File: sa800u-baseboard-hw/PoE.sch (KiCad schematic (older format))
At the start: 23 parts

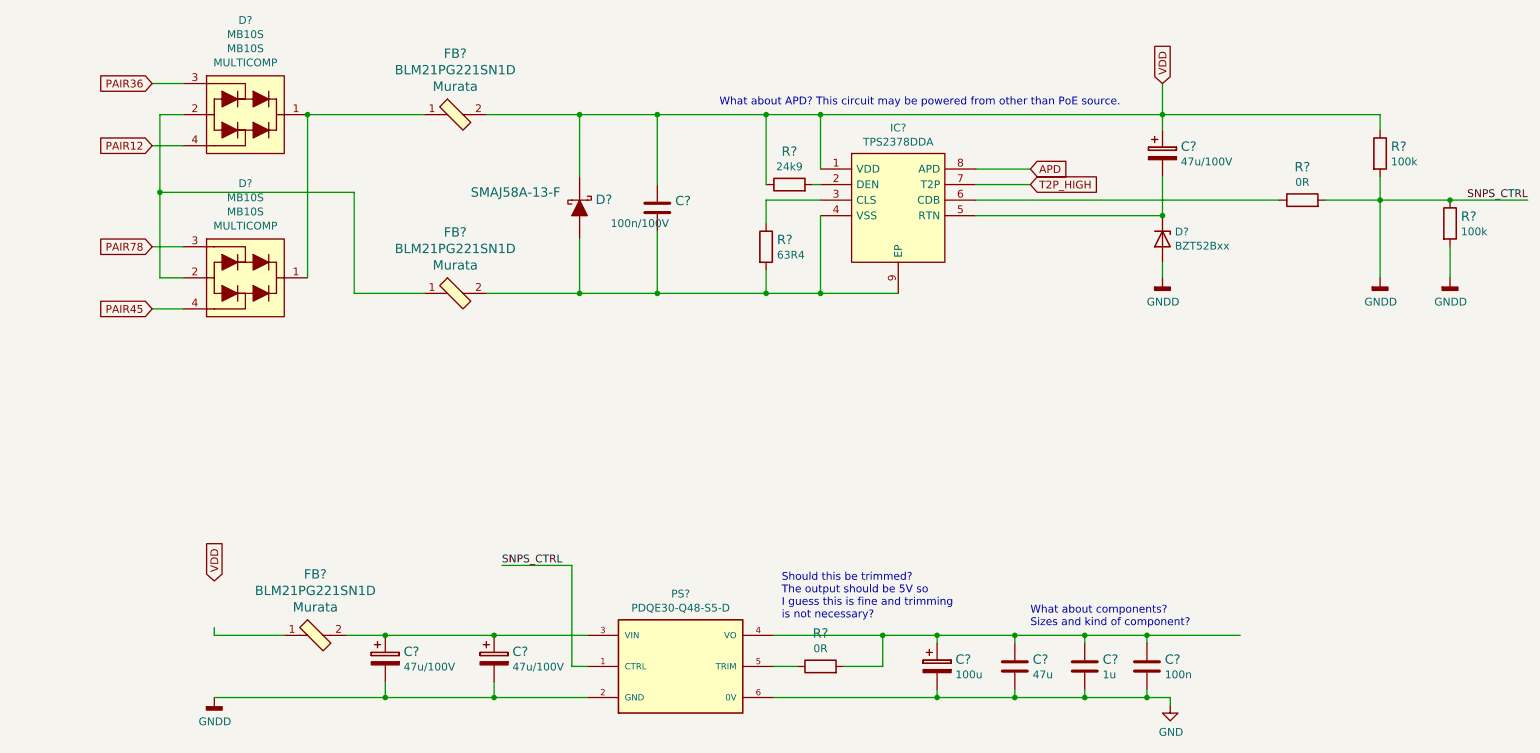
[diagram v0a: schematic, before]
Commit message: added initial version of ethernet controller
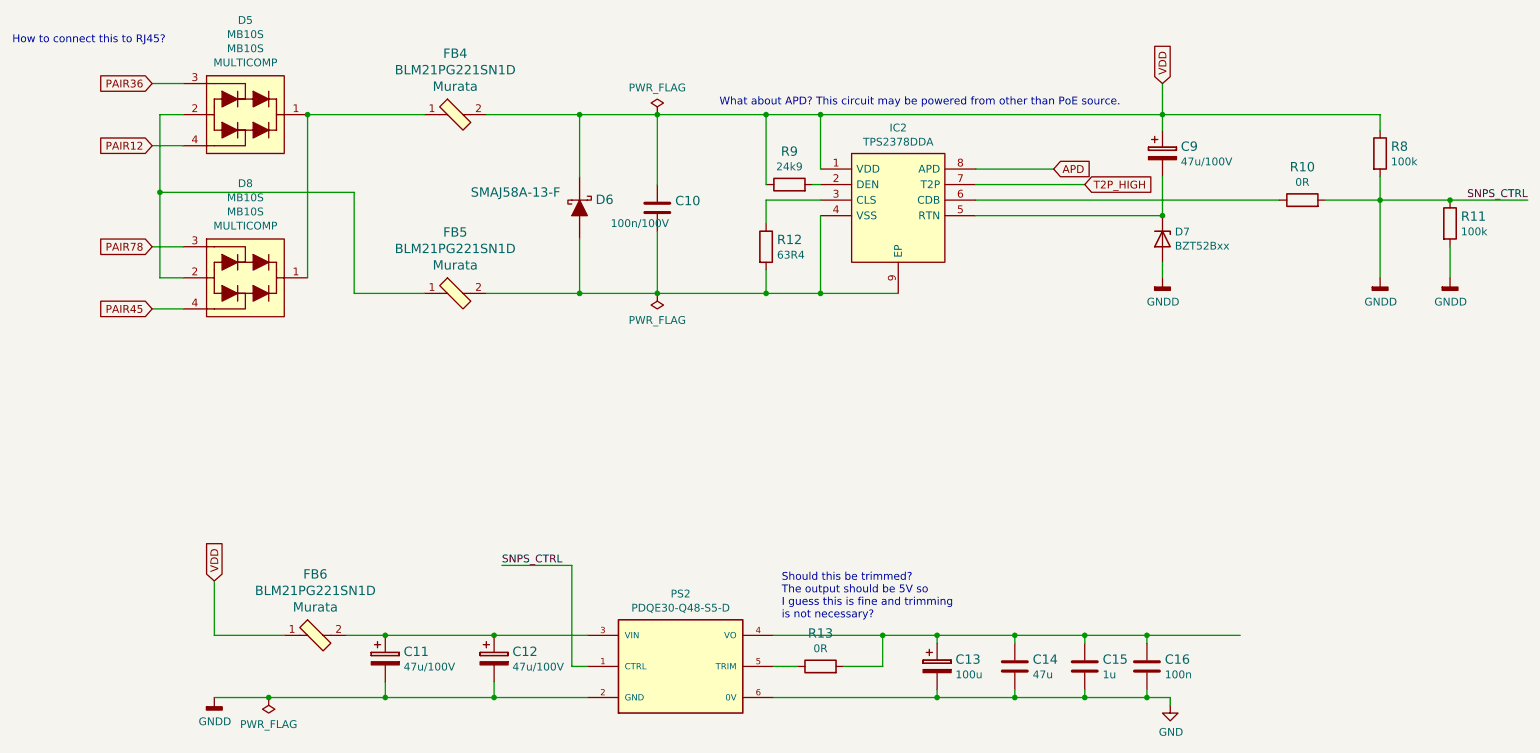
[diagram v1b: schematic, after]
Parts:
- gave numbers to parts that had none: 23
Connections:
- net VDD: now also FB6.1
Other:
- note added: "How to connect this to RJ45?"
- note removed: "What about components? \nSizes and kind of component?"

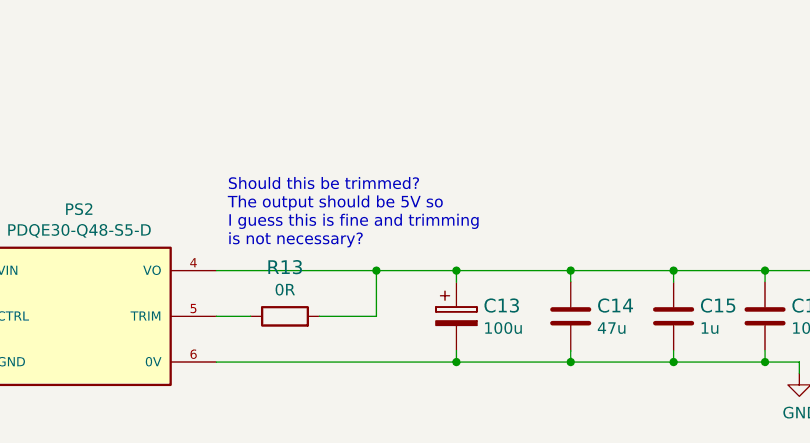
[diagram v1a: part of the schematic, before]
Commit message: added a voltage trimming possibility in PoE circuit
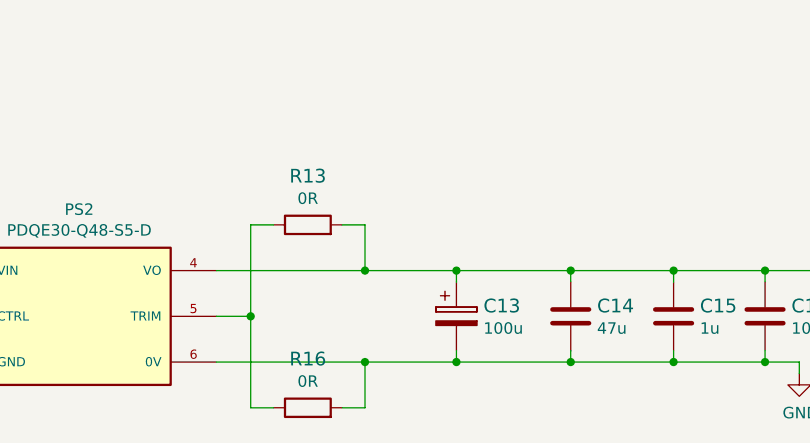
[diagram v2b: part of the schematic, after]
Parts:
- added R16: R_0R_0402, antmicro-footprints:0402-res, symbol antmicroResistors0402:R_0R_0402
- R13: DNP (none) -> DNP
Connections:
- net GND: now also R16.2
- net at PS2.5 (TRIM), R13.1: now also R16.1
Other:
- note removed: "Should this be trimmed? \nThe output should be 5V so\nI guess this is fine and trimming\nis not necessary?"
- moved on the sheet: R13
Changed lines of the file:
@@
 Wire Wire Line
 	1450 2600 1650 2600
-Text Notes 5500 5000 0    50   ~ 0
-Should this be trimmed? \nThe output should be 5V so\nI guess this is fine and trimming\nis not necessary?
 $Comp
 L power:GND #PWR010
@@
 	8000 5500 8000 5550
 Wire Wire Line
-	5450 5500 6500 5500
+	5450 5500 6100 5500
 Wire Wire Line
 	5600 5300 5450 5300
@@
 L antmicroResistors0402:R_0R_0402 R13
 U 1 1 61A460AF
-P 5750 5300
-F 0 "R13" H 5750 5513 60  0000 C CNN
-F 1 "R_0R_0402" H 5750 5150 60  0001 C CNN
-F 2 "antmicro-footprints:0402-res" H 5950 5500 60  0001 L CNN
-F 3 "" H 5750 5300 50  0001 C CNN
-F 4 "PANASONIC" H 5950 5700 60  0001 L CNN "Manufacturer"
-F 5 "ERJ2GE0R00X" H 5950 5600 60  0001 L CNN "MPN"
-F 6 "0R" H 5750 5415 50  0000 C CNN "Val"
-	1    5750 5300
-	1    0    0    -1
-$EndComp
-Wire Wire Line
-	6150 5100 6500 5100
-Connection ~ 6150 5100
-Wire Wire Line
-	6150 5300 5900 5300
-Wire Wire Line
-	6150 5100 6150 5300
-Wire Wire Line
-	5450 5100 6150 5100
+P 5850 4900
+F 0 "R13" H 5850 5113 60  0000 C CNN
+F 1 "R_0R_0402" H 5850 4750 60  0001 C CNN
+F 2 "antmicro-footprints:0402-res" H 6050 5100 60  0001 L CNN
+F 3 "" H 5850 4900 50  0001 C CNN
+F 4 "PANASONIC" H 6050 5300 60  0001 L CNN "Manufacturer"
+F 5 "ERJ2GE0R00X" H 6050 5200 60  0001 L CNN "MPN"
+F 6 "0R" H 5850 5015 50  0000 C CNN "Val"
+F 7 "DNP" H 5850 4900 50  0001 C CNN "DNP"
+	1    5850 4900
+	1    0    0    -1
+$EndComp
 Text GLabel 7250 2100 2    50   Input ~ 0
 APD
@@
 	-1   0    0    1
 $EndComp
+$Comp
+L antmicroResistors0402:R_0R_0402 R16
+U 1 1 6197A6CB
+P 5850 5700
+F 0 "R16" H 5850 5913 60  0000 C CNN
+F 1 "R_0R_0402" H 5850 5550 60  0001 C CNN
+F 2 "antmicro-footprints:0402-res" H 6050 5900 60  0001 L CNN
+F 3 "" H 5850 5700 50  0001 C CNN
+F 4 "PANASONIC" H 6050 6100 60  0001 L CNN "Manufacturer"
+F 5 "ERJ2GE0R00X" H 6050 6000 60  0001 L CNN "MPN"
+F 6 "0R" H 5850 5815 50  0000 C CNN "Val"
+F 7 "DNP" H 5850 5700 50  0001 C CNN "DNP"
+	1    5850 5700
+	1    0    0    -1
+$EndComp
+Wire Wire Line
+	5600 5300 5600 5700
+Wire Wire Line
+	5600 5700 5700 5700
+Connection ~ 5600 5300
+Wire Wire Line
+	5450 5100 6100 5100
+Wire Wire Line
+	6000 5700 6100 5700
+Wire Wire Line
+	6100 5700 6100 5500
+Connection ~ 6100 5500
+Wire Wire Line
+	6100 5500 6500 5500
+Connection ~ 6100 5100
+Wire Wire Line
+	6100 5100 6500 5100
+Wire Wire Line
+	5600 4900 5700 4900
+Wire Wire Line
+	5600 4900 5600 5300
+Wire Wire Line
+	6000 4900 6100 4900
+Wire Wire Line
+	6100 4900 6100 5100
 $EndSCHEMATC
